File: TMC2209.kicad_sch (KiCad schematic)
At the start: 27 parts, among them J3 Conn_01x04_Male, U3 TMC2209-LA

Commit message: Rename files Remove unnecessary contents
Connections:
- net +3V3: now also U3.15 (VCC_IO); no longer U3.5 (CPI)
- net GND: now also U3.18 (GND), U3.3 (GND)
- net VCC: now also U3.22 (VS), U3.28 (VS); no longer U3.20 (STDBY), U3.7 (SPREAD)
- net Vref: now also U3.17 (VREF); no longer U3.2 (ENN)
- net chargePumpVoltage: now also U3.6 (VCP); no longer U3.19 (DIR)
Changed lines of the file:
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@@
     (pin "8")
     (pin "9")
+    (pin "15")
+    (pin "17")
+    (pin "18")
+    (pin "22")
+    (pin "25")
+    (pin "28")
+    (pin "3")
+    (pin "6")
   )
-  (symbol (lib_id "tmc2209:TMC2209-LA") (at 140.97 82.55 0) (unit 1)
+  (symbol (lib_id "tmc2209:TMC2209-LA") (at 140.97 82.55 0) (unit 2)
     (in_bom yes) (on_board yes)
     (property "Reference" "U3" (id 0) (at 161.29 72.7202 0)
@@
     (pin "8")
     (pin "9")
+    (pin "15")
+    (pin "17")
+    (pin "18")
+    (pin "22")
+    (pin "25")
+    (pin "28")
+    (pin "3")
+    (pin "6")
   )
   (symbol (lib_id "Connector:Conn_01x04_Male") (at 273.05 78.74 180) (unit 1)

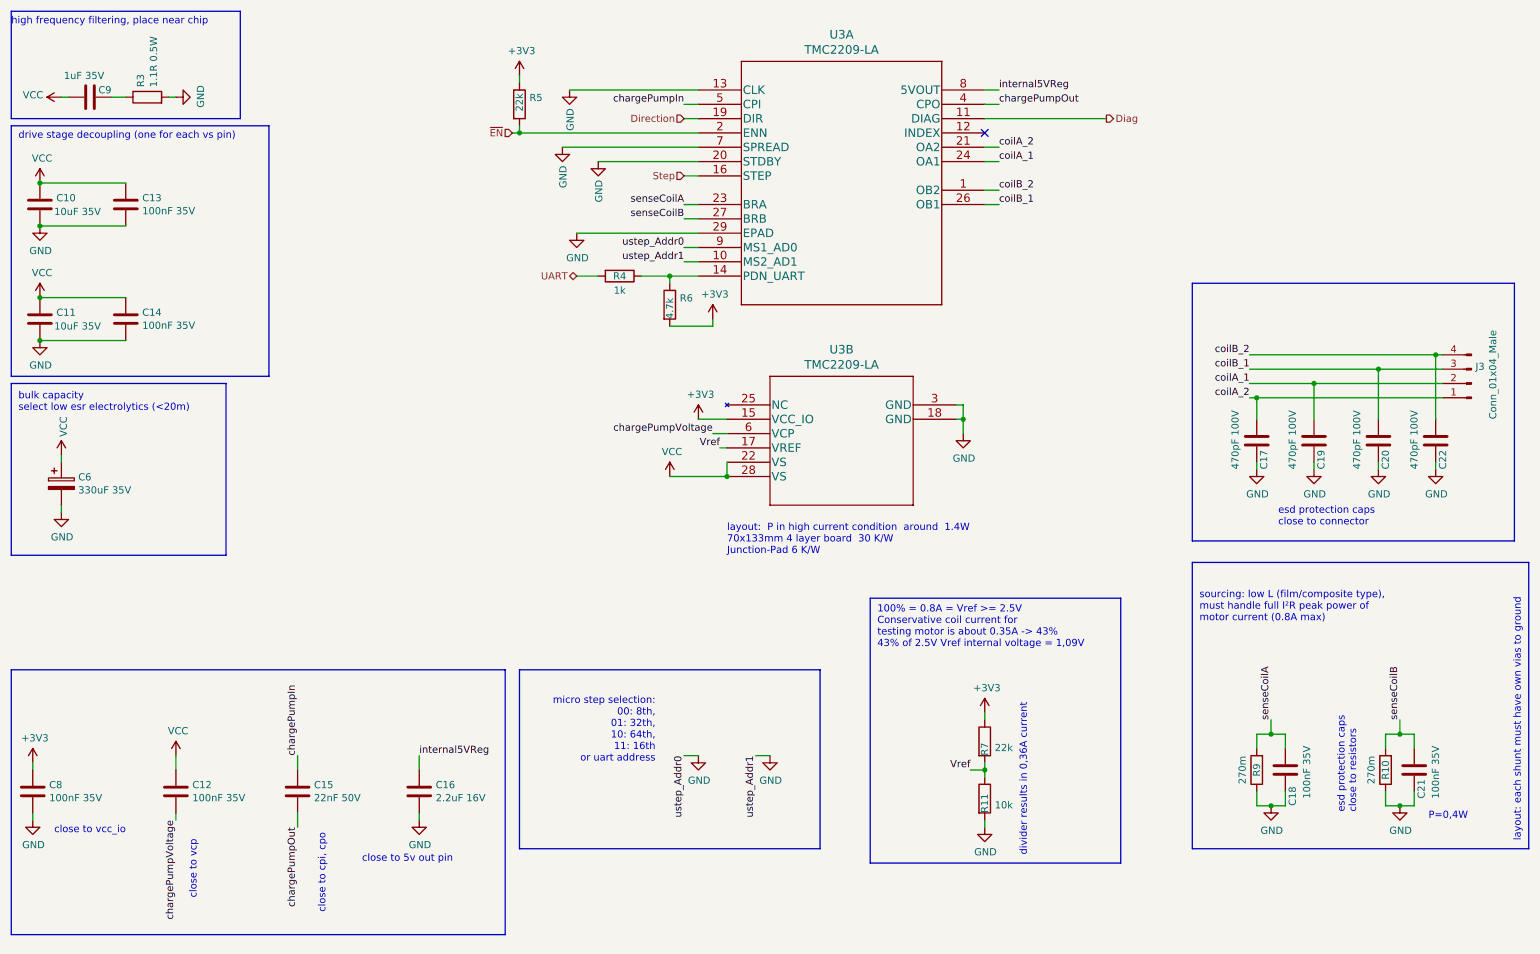
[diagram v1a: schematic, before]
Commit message: Rearrange schematic and some cleanups Add 5V buck converter Update values for TMC2209 Add EEPROM Switch to STM32G0B1KE
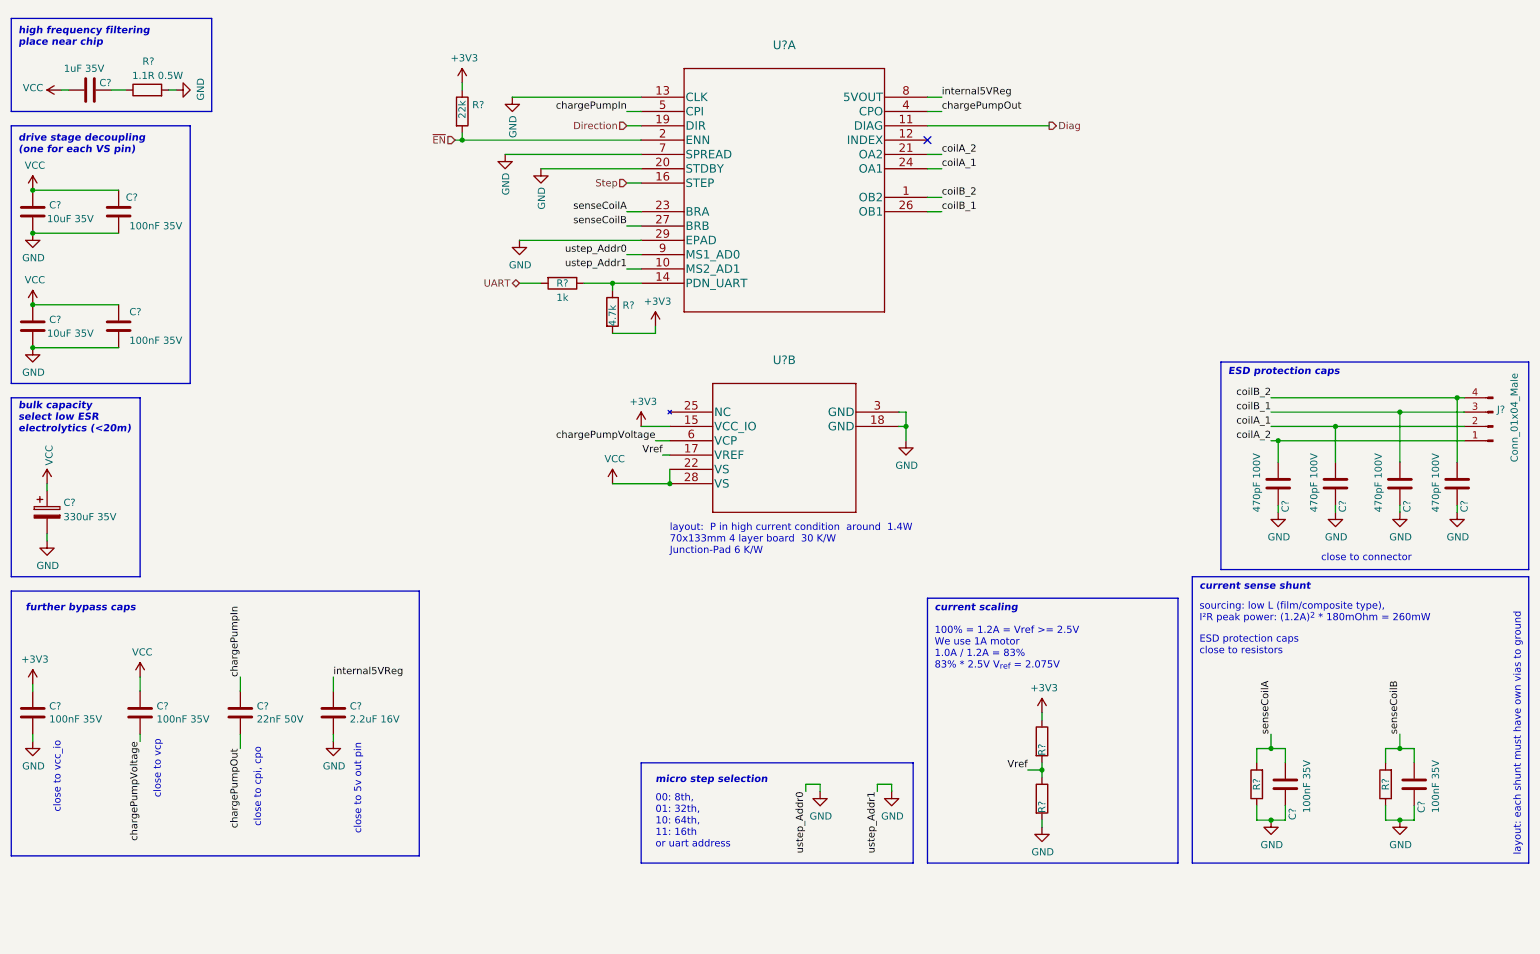
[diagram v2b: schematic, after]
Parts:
- removed C6: 330uF 35V, Capacitor_SMD:CP_Elec_10x10.5, symbol Device:CP
- removed U3: TMC2209-LA, Package_DFN_QFN:QFN-28-1EP_5x5mm_P0.5mm_EP3.35x3.35mm_ThermalVias, symbol tmc2209:TMC2209-LA
- added C?: 330uF 35V, Capacitor_SMD:CP_Elec_10x10.5, symbol Device:C_Polarized
- added U?: (no value), symbol extraSymbols:TMC2209-LA
- added U?: (no value), Package_DFN_QFN:QFN-28-1EP_5x5mm_P0.5mm_EP3.35x3.35mm_ThermalVias, symbol extraSymbols:TMC2209-LA
- R?: renamed from R9; value 270m -> (none)
- R?: renamed from R10; value 270m -> (none)
- R?: renamed from R7; value 22k -> (none)
- R?: renamed from R11; value 10k -> (none)
- renumbered C15 to C?, C12 to C?, C16 to C?, C8 to C?, C18 to C?, C21 to C?, C17 to C?, C19 to C?, C20 to C?, C22 to C?, C13 to C?, C10 to C?, C9 to C?, C14 to C?, C11 to C?, J3 to J?, R3 to R?, R5 to R?, R6 to R?, R4 to R?
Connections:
- net +3V3: now also U?.15 (VCC_IO)
- net Diag: now also U?.11 (DIAG)
- net Direction: now also U?.19 (DIR)
- net GND: now also C?.2, U?.10 (MS2_AD1), U?.13 (CLK), U?.18 (GND), U?.20 (STDBY), U?.29 (EPAD), U?.3 (GND), U?.7 (SPREAD), U?.9 (MS1_AD0)
- net Step: now also U?.16 (STEP)
- net VCC: now also C?.1, U?.22 (VS), U?.28 (VS)
- net Vref: now also U?.17 (VREF)
- net chargePumpIn: now also U?.5 (CPI)
- net chargePumpOut: now also U?.4 (CPO)
- net chargePumpVoltage: now also U?.6 (VCP)
- net coilA_1: now also U?.24 (OA1)
- net coilA_2: now also U?.21 (OA2)
- net coilB_1: now also U?.26 (OB1)
- net coilB_2: now also U?.1 (OB2)
- net internal5VReg: now also U?.8 (5VOUT)
- net senseCoilA: now also U?.23 (BRA)
- net senseCoilB: now also U?.27 (BRB)
- net ~{EN}: now also U?.2 (ENN)
- net at R?.1, R?.1: now also U?.14 (PDN_UART)
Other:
- note added: "00: 8th, 01: 32th, 10: 64th, 11: 16th or uart address"
- note added: "100% = 1.2A = Vref >= 2.5V We use 1A motor 1.0A / 1.2A = 83% 83% * 2.5V V_{ref} = 2.075V"
- note added: "ESD protection caps"
- note added: "ESD protection caps close to resistors"
- note added: "bulk capacity select low ESR electrolytics (<20m)"
- note added: "close to connector"
- note added: "current scaling"
- note added: "current sense shunt"
- note added: "drive stage decoupling (one for each VS pin)"
- note added: "further bypass caps"
- note added: "high frequency filtering place near chip"
- note added: "micro step selection"
- note added: "sourcing: low L (film/composite type), I²R peak power: (1.2A)^{2} * 180mOhm = 260mW"
- note removed: "100% = 0.8A = Vref >= 2.5V Conservative coil current for testing motor is about 0.35A -> 43% 43% of 2.5V Vref internal voltage = 1,09V"
- note removed: "P=0,4W"
- note removed: "bulk capacity select low esr electrolytics (<20m)"
- note removed: "divider results in 0,36A current"
- note removed: "drive stage decoupling (one for each vs pin)"
- note removed: "esd protection caps close to connector"
- note removed: "esd protection caps close to resistors"
- note removed: "high frequency filtering, place near chip"
- note removed: "micro step selection: 00: 8th, 01: 32th, 10: 64th, 11: 16th or uart address"
- note removed: "sourcing: low L (film/composite type), must handle full I²R peak power of motor current (0.8A max)"
- moved on the sheet: C?, J?, R?

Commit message: Small changes
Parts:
- R? (x2): value (none) -> 180m
- R?: value (none) -> 13k
- R?: value (none) -> 22k
- U?: value (none) -> TMC2209-LA; footprint (none) -> Package_DFN_QFN:QFN-28-1EP_5x5mm_P0.5mm_EP3.35x3.35mm_ThermalVias
- U?: value (none) -> TMC2209-LA
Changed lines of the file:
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@@
     (in_bom yes) (on_board yes)
     (property "Reference" "R?" (id 0) (at 234.95 149.86 90))
-    (property "Value" "" (id 1) (at 232.41 149.86 90))
+    (property "Value" "180m" (id 1) (at 232.41 149.86 90))
     (property "Footprint" "Resistor_SMD:R_0612_1632Metric" (id 2) (at 236.728 149.86 90)
       (effects (font (size 1.27 1.27)) hide)
@@
     (in_bom yes) (on_board yes)
     (property "Reference" "R?" (id 0) (at 257.81 149.86 90))
-    (property "Value" "" (id 1) (at 255.27 149.86 90))
+    (property "Value" "180m" (id 1) (at 255.27 149.86 90))
     (property "Footprint" "Resistor_SMD:R_0612_1632Metric" (id 2) (at 259.588 149.86 90)
       (effects (font (size 1.27 1.27)) hide)
@@
       (effects (font (size 1.27 1.27)) (justify left))
     )
-    (property "Value" "" (id 1) (at 198.628 143.383 0)
+    (property "Value" "13k" (id 1) (at 198.628 143.383 0)
       (effects (font (size 1.27 1.27)) (justify left))
     )
@@
       (effects (font (size 1.27 1.27)) (justify left))
     )
-    (property "Value" "" (id 1) (at 198.628 153.543 0)
+    (property "Value" "22k" (id 1) (at 198.628 153.543 0)
       (effects (font (size 1.27 1.27)) (justify left))
     )
@@
       (effects (font (size 1.524 1.524)))
     )
-    (property "Value" "" (id 1) (at 151.13 21.7058 0)
+    (property "Value" "TMC2209-LA" (id 1) (at 151.13 21.7058 0)
       (effects (font (size 1.524 1.524)))
     )
-    (property "Footprint" "" (id 2) (at 151.13 21.844 0)
+    (property "Footprint" "Package_DFN_QFN:QFN-28-1EP_5x5mm_P0.5mm_EP3.35x3.35mm_ThermalVias" (id 2) (at 151.13 21.844 0)
       (effects (font (size 1.524 1.524)) hide)
     )
@@
       (effects (font (size 1.524 1.524)))
     )
-    (property "Value" "" (id 1) (at 151.13 77.5858 0)
+    (property "Value" "TMC2209-LA" (id 1) (at 151.13 77.5858 0)
       (effects (font (size 1.524 1.524)))
     )

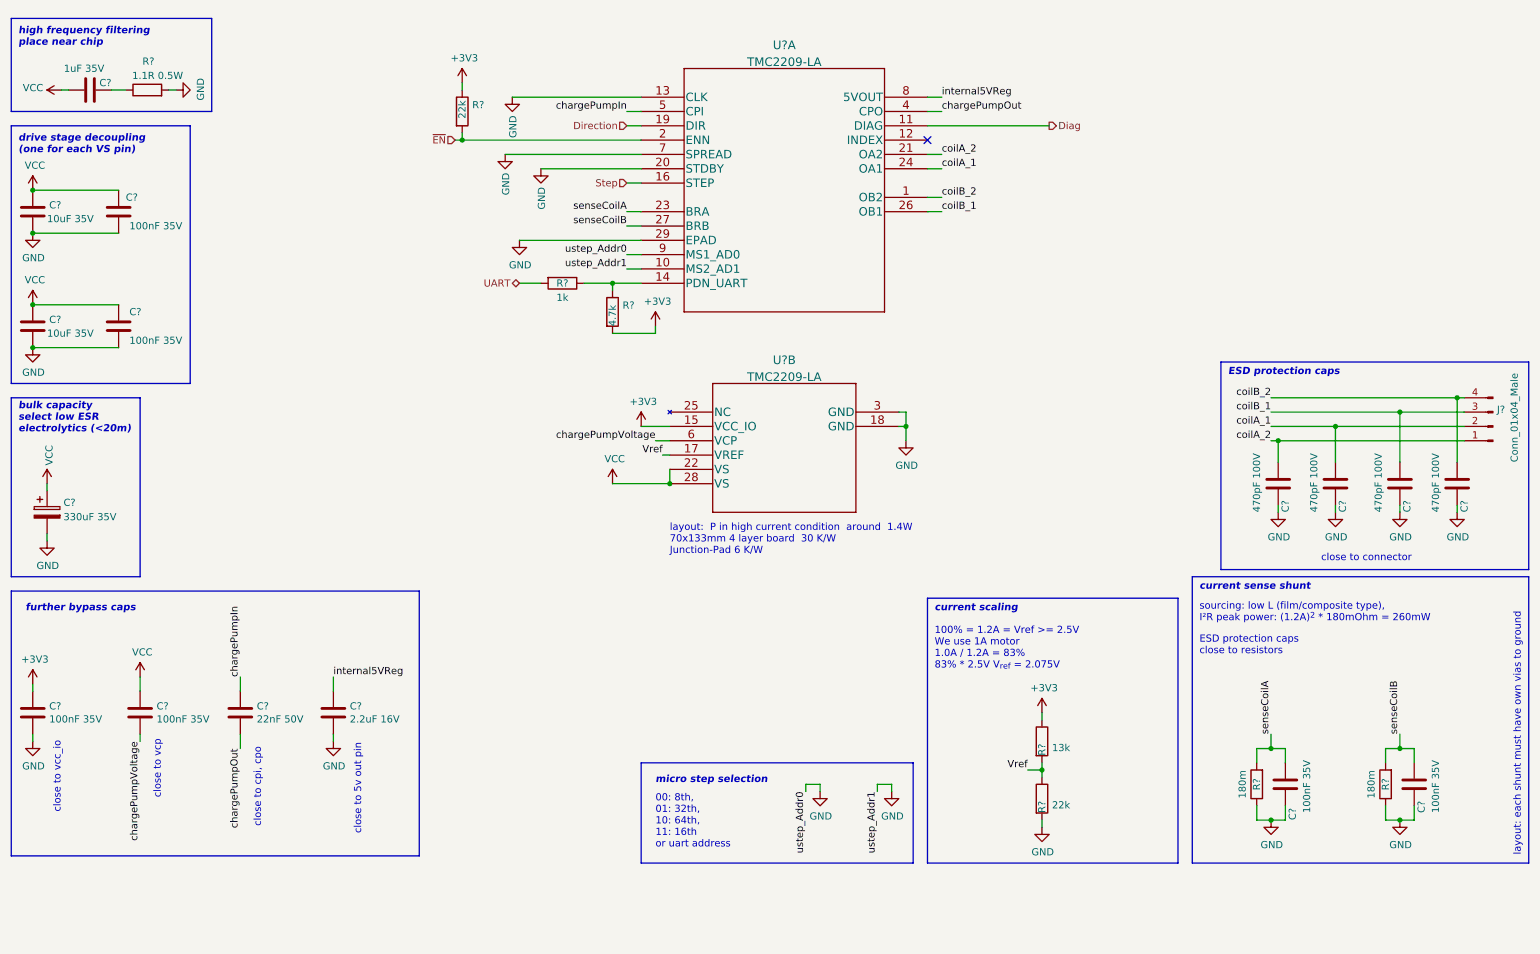
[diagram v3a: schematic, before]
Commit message: Annotate symbols and assign footprints
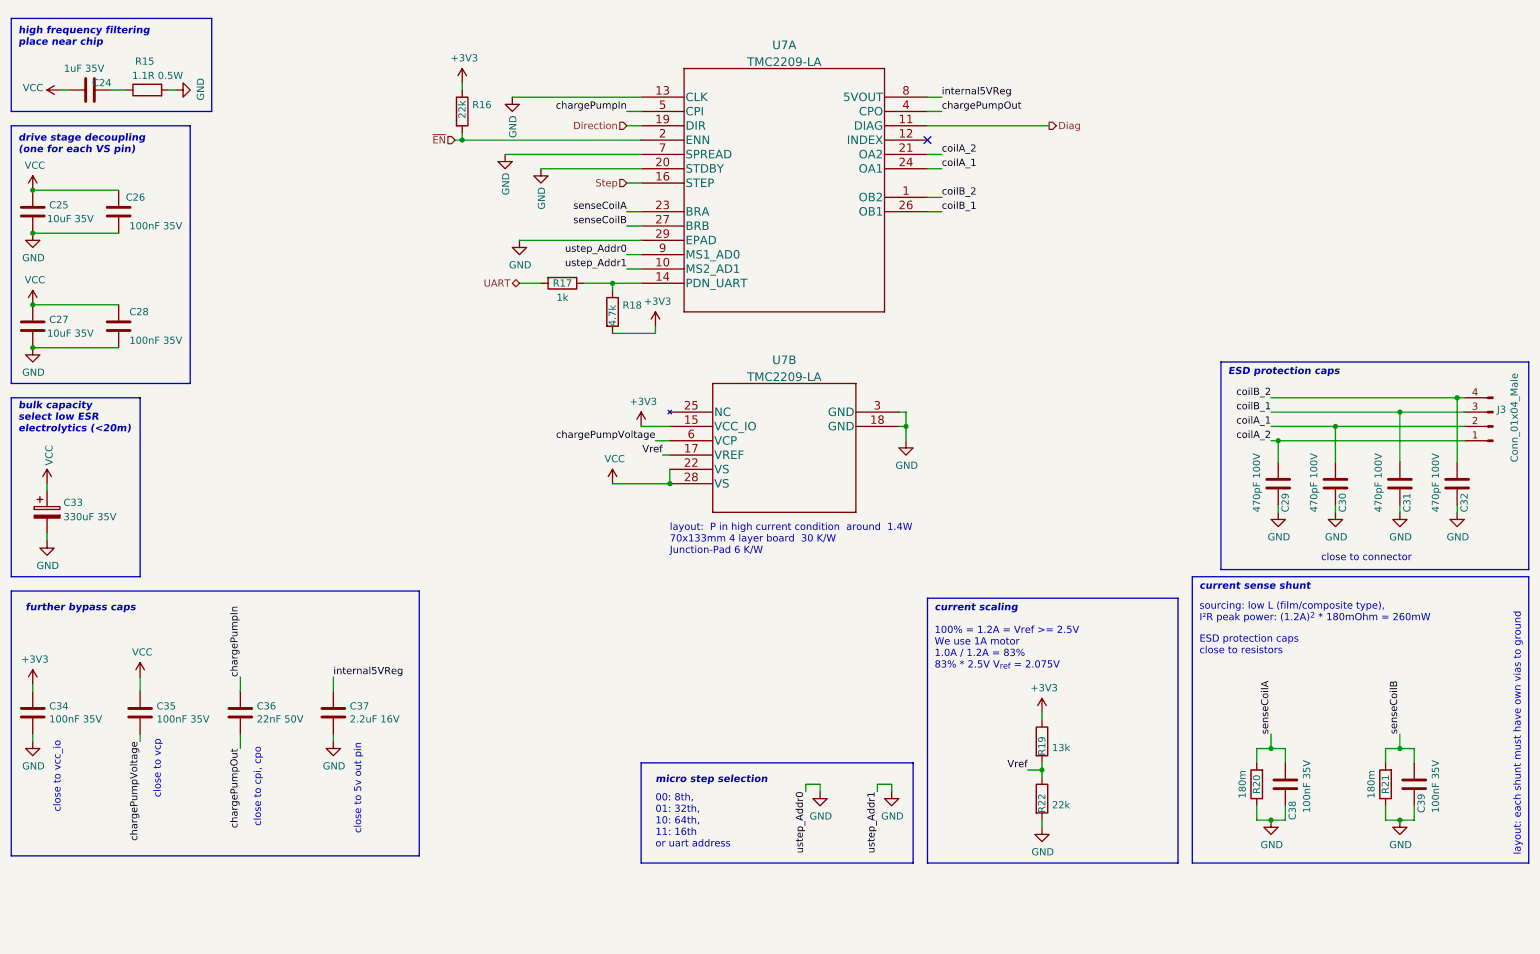
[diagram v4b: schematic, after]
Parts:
- gave numbers to parts that had none: 26
